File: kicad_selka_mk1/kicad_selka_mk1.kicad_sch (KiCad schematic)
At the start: 76 parts, among them J1 Conn_01x06_Pin, J2 Conn_01x02_Pin, U1 ATtiny861A-S

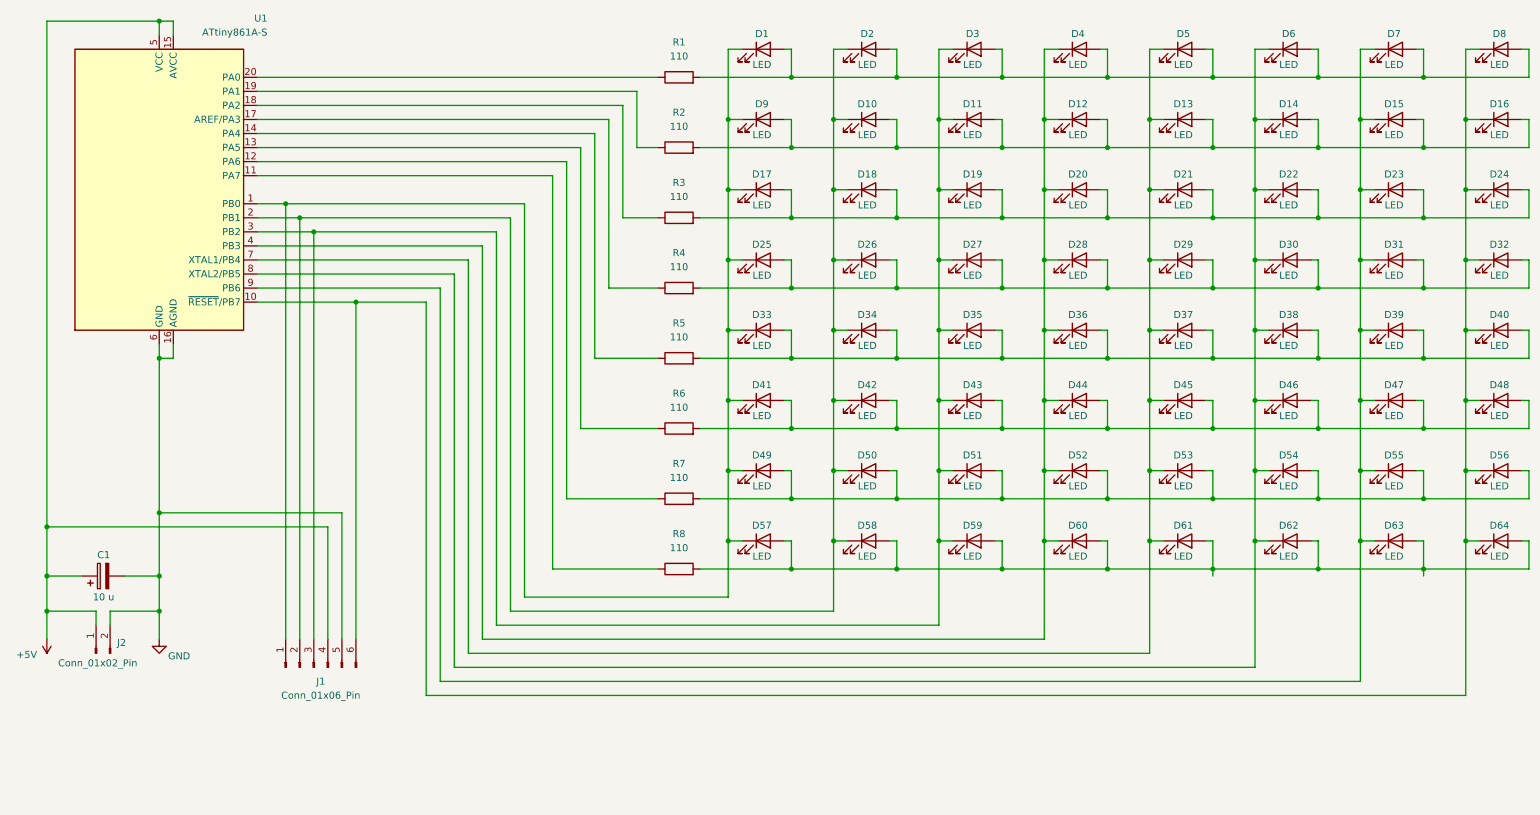
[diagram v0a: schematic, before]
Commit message: Selkäsalaman skemaan lisätty jumperit
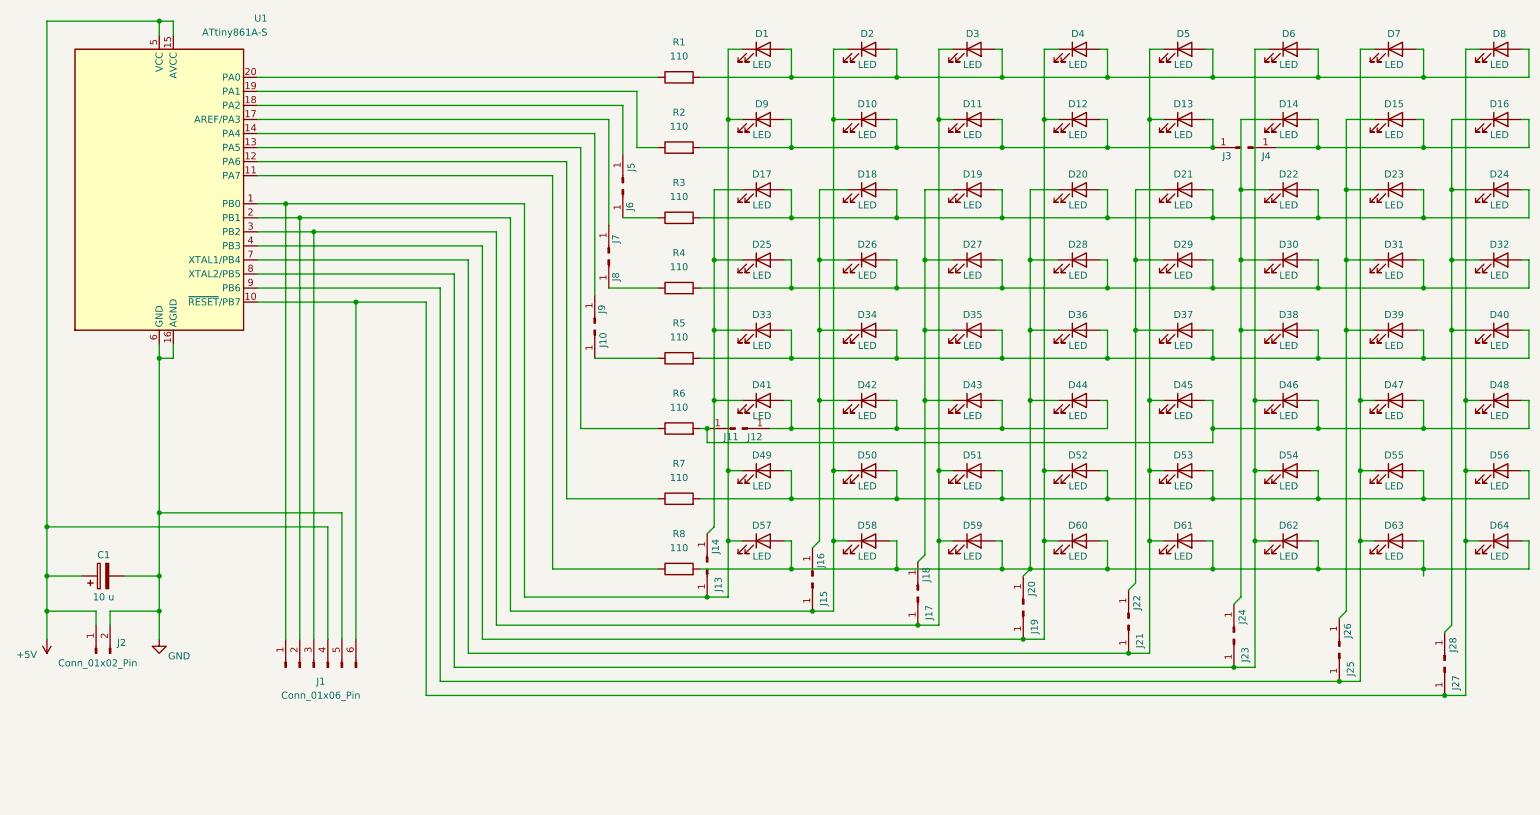
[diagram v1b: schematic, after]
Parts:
- added J10, J11, J12, J13, J14, J15, J16, J17, J18, J19, J20, J21, J22, J23, J24, J25, J26, J27, J28, J3, J4, J5, J6, J7, J8, J9: Conn_01x01_Pin, Connector_PinSocket_2.54mm:PinSocket_1x01_P2.54mm_Vertical, symbol Connector:Conn_01x01_Pin
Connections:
- net at D13.1 (K), D45.1 (K), D5.1 (K)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: now also J21.1 (Pin_1); no longer D21.1 (K), D29.1 (K), D37.1 (K)
- net at D11.1 (K), D3.1 (K), D51.1 (K)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: now also J17.1 (Pin_1); no longer D19.1 (K), D27.1 (K), D35.1 (K), D43.1 (K)
- net at D12.1 (K), D4.1 (K), D52.1 (K)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: now also J19.1 (Pin_1); no longer D20.1 (K), D28.1 (K), D36.1 (K), D44.1 (K)
- net at D10.1 (K), D2.1 (K), D50.1 (K)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: now also J15.1 (Pin_1); no longer D18.1 (K), D26.1 (K), D34.1 (K), D42.1 (K)
- net at D57.2 (A), D58.2 (A), D59.2 (A)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: now also D20.1 (K), D28.1 (K), D36.1 (K), D44.1 (K), J20.1 (Pin_1)
- net at D48.1 (K), D56.1 (K), D64.1 (K)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: now also J27.1 (Pin_1); no longer D16.1 (K), D24.1 (K), D32.1 (K), D40.1 (K)
- net at D47.1 (K), D55.1 (K), D63.1 (K)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: now also J25.1 (Pin_1); no longer D15.1 (K), D23.1 (K), D31.1 (K), D39.1 (K)
- net at D46.1 (K), D54.1 (K), D6.1 (K)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: now also J23.1 (Pin_1); no longer D14.1 (K), D22.1 (K), D30.1 (K), D38.1 (K)
- net at R4.1: now also J8.1 (Pin_1); no longer U1.17 (AREF/PA3)
- net at D45.2 (A), D46.2 (A), D47.2 (A)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: now also J11.1 (Pin_1); no longer D41.2 (A), D42.2 (A), D43.2 (A), D44.2 (A)
- net at D10.2 (A), D11.2 (A), D12.2 (A)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: now also J3.1 (Pin_1); no longer D14.2 (A), D15.2 (A), D16.2 (A)
- net at D1.1 (K), D49.1 (K), D57.1 (K)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: now also J13.1 (Pin_1); no longer D17.1 (K), D25.1 (K), D33.1 (K), D41.1 (K)
- net at R3.1: now also J6.1 (Pin_1); no longer U1.18 (PA2)
- net at R5.1: now also J10.1 (Pin_1); no longer U1.14 (PA4)
- new net: D21.1 (K), D29.1 (K), D37.1 (K), J22.1 (Pin_1)
- new net: D19.1 (K), D27.1 (K), D35.1 (K), D43.1 (K), J18.1 (Pin_1)
- new net: D18.1 (K), D26.1 (K), D34.1 (K), D42.1 (K), J16.1 (Pin_1)
- new net: D16.1 (K), D24.1 (K), D32.1 (K), D40.1 (K), J28.1 (Pin_1)
- new net: D14.1 (K), D22.1 (K), D30.1 (K), D38.1 (K), J24.1 (Pin_1)
- new net: D41.2 (A), D42.2 (A), D43.2 (A), D44.2 (A), J12.1 (Pin_1)
- new net: D17.1 (K), D25.1 (K), D33.1 (K), D41.1 (K), J14.1 (Pin_1)
- new net: D14.2 (A), D15.2 (A), D16.2 (A), J4.1 (Pin_1)
- new net: D15.1 (K), D23.1 (K), D31.1 (K), D39.1 (K), J26.1 (Pin_1)
- new net: J9.1 (Pin_1), U1.14 (PA4)
- new net: J5.1 (Pin_1), U1.18 (PA2)
- new net: J7.1 (Pin_1), U1.17 (AREF/PA3)

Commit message: Selkäsalama 95% done
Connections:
- net at D57.2 (A), D58.2 (A), D59.2 (A)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: no longer D20.1 (K), D28.1 (K), D36.1 (K), D44.1 (K), J20.1 (Pin_1)
- new net: D20.1 (K), D28.1 (K), D36.1 (K), D44.1 (K), J20.1 (Pin_1)
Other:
- note added: "CYAANI ALUE = Alempi Levy"
- moved on the sheet: J10, J11, J12, J13, J14, J15, J16, J17, J18, J19, J20, J21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

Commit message: Selkäsalama redo
1 ledi meni väärälle puolelle -> 31 & 33 lediä :C

Samahan se oli tehdä koko leiska uudelleen parammilla array
ledipaikoilla...
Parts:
- added R9: 110, Resistor_SMD:R_1206_3216Metric_Pad1.30x1.75mm_HandSolder, symbol Device:R
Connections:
- net +5V: now also R9.1
- net GND: now also R9.2
- net at D21.1 (K), D29.1 (K), D37.1 (K)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: now also D45.1 (K)
- net at D13.1 (K), D5.1 (K), D53.1 (K)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: no longer D45.1 (K)
- net at D41.2 (A), D42.2 (A), D43.2 (A)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: now also D45.2 (A)
- net at D46.2 (A), D47.2 (A), D48.2 (A)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: no longer D45.2 (A)
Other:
- title: Salama-64 -> Selkäsalama-64
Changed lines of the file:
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@@
 	(paper "User" 330.2 203.2)
 	(title_block
-		(title "Salama-64")
+		(title "Selkäsalama-64")
 		(date "2026-02-12")
 		(company "ELEKTRONIIKKAKERHO")
@@
 	)
 	(junction
+		(at 226.06 92.71)
+		(diameter 0)
+		(color 0 255 255 1)
+	)
+	(junction
 		(at 290.83 97.79)
 		(diameter 0)
@@
 	)
 	(junction
+		(at 54.61 115.57)
+		(diameter 0)
+		(color 0 0 0 0)
+	)
+	(junction
 		(at 193.04 138.43)
 		(diameter 0)
@@
 	)
 	(junction
-		(at 233.68 97.79)
-		(diameter 0)
-		(color 0 0 0 0)
-	)
-	(junction
 		(at 154.94 85.09)
 		(diameter 0)
@@
 	)
 	(junction
+		(at 34.29 115.57)
+		(diameter 0)
+		(color 0 0 0 0)
+	)
+	(junction
 		(at 212.09 97.79)
 		(diameter 0)
@@
 	)
 	(junction
-		(at 245.11 102.87)
-		(diameter 0)
-		(color 0 0 0 0)
-	)
-	(junction
 		(at 154.94 72.39)
 		(diameter 0)
@@
 	)
 	(junction
+		(at 231.14 97.79)
+		(diameter 0)
+		(color 0 255 255 1)
+	)
+	(junction
 		(at 252.73 97.79)
 		(diameter 0)
@@
 	(wire
 		(pts
-			(xy 233.68 97.79) (xy 236.22 97.79)
-		)
-		(stroke
-			(width 0)
-			(type default)
-		)
-	)
-	(wire
-		(pts
 			(xy 283.21 102.87) (xy 302.26 102.87)
 		)
@@
 	(wire
 		(pts
-			(xy 233.68 46.99) (xy 233.68 97.79)
-		)
-		(stroke
-			(width 0)
-			(type default)
-		)
-	)
-	(wire
-		(pts
 			(xy 264.16 115.57) (xy 283.21 115.57)
 		)
@@
 			(width 0)
 			(type default)
+			(color 0 255 255 1)
 		)
 	)
@@
 	(wire
 		(pts
+			(xy 231.14 97.79) (xy 236.22 97.79)
+		)
+		(stroke
+			(width 0)
+			(type default)
+			(color 0 255 255 1)
+		)
+	)
+	(wire
+		(pts
 			(xy 135.89 52.07) (xy 139.7 52.07)
 		)
@@
 	(wire
 		(pts
+			(xy 245.11 92.71) (xy 245.11 97.79)
+		)
+		(stroke
+			(width 0)
+			(type default)
+			(color 0 255 255 1)
+		)
+	)
+	(wire
+		(pts
 			(xy 168.91 90.17) (xy 187.96 90.17)
 		)
@@
 	(wire
 		(pts
+			(xy 34.29 115.57) (xy 40.64 115.57)
+		)
+		(stroke
+			(width 0)
+			(type default)
+		)
+	)
+	(wire
+		(pts
 			(xy 72.39 77.47) (xy 100.33 77.47)
 		)
@@
 	(wire
 		(pts
+			(xy 54.61 90.17) (xy 54.61 115.57)
+		)
+		(stroke
+			(width 0)
+			(type default)
+		)
+	)
+	(wire
+		(pts
 			(xy 72.39 49.53) (xy 128.27 49.53)
 		)
@@
 	(wire
 		(pts
+			(xy 34.29 29.21) (xy 34.29 115.57)
+		)
+		(stroke
+			(width 0)
+			(type default)
+		)
+	)
+	(wire
+		(pts
 			(xy 130.81 77.47) (xy 139.7 77.47)
 		)
@@
 	(wire
 		(pts
-			(xy 149.86 102.87) (xy 245.11 102.87)
+			(xy 149.86 102.87) (xy 264.16 102.87)
 		)
 		(stroke
@@
 	(wire
 		(pts
+			(xy 48.26 115.57) (xy 54.61 115.57)
+		)
+		(stroke
+			(width 0)
+			(type default)
+		)
+	)
+	(wire
+		(pts
 			(xy 226.06 64.77) (xy 245.11 64.77)
 		)
@@
 	(wire
 		(pts
+			(xy 226.06 92.71) (xy 245.11 92.71)
+		)
+		(stroke
+			(width 0)
+			(type default)
+			(color 0 255 255 1)
+		)
+	)
+	(wire
+		(pts
 			(xy 283.21 123.19) (xy 283.21 128.27)
 		)
@@
 	(wire
 		(pts
-			(xy 231.14 85.09) (xy 231.14 132.08)
+			(xy 231.14 85.09) (xy 231.14 97.79)
 		)
 		(stroke
@@
 	(wire
 		(pts
-			(xy 34.29 120.65) (xy 34.29 29.21)
+			(xy 34.29 120.65) (xy 34.29 115.57)
 		)
 		(stroke
@@
 	(wire
 		(pts
-			(xy 233.68 97.79) (xy 233.68 110.49)
+			(xy 233.68 46.99) (xy 233.68 110.49)
 		)
 		(stroke
@@
 	(wire
 		(pts
-			(xy 54.61 118.11) (xy 54.61 90.17)
+			(xy 54.61 118.11) (xy 54.61 115.57)
 		)
 		(stroke
@@
 	(wire
 		(pts
+			(xy 231.14 97.79) (xy 231.14 132.08)
+		)
+		(stroke
+			(width 0)
+			(type default)
+			(color 0 255 255 1)
+		)
+	)
+	(wire
+		(pts
 			(xy 123.19 115.57) (xy 139.7 115.57)
 		)
@@
 	(wire
 		(pts
-			(xy 245.11 97.79) (xy 245.11 102.87)
-		)
-		(stroke
-			(width 0)
-			(type default)
-		)
-	)
-	(wire
-		(pts
 			(xy 102.87 146.05) (xy 250.19 146.05)
 		)
@@
 	(wire
 		(pts
-			(xy 245.11 102.87) (xy 264.16 102.87)
-		)
-		(stroke
-			(width 0)
-			(type default)
-		)
-	)
-	(wire
-		(pts
 			(xy 207.01 46.99) (xy 207.01 52.07)
 		)
@@
 			(pts
 				(xy 304.8 41.91) (xy 248.92 41.91) (xy 248.92 43.18) (xy 248.92 54.61) (xy 152.4 54.61) (xy 152.4 59.69)
-				(xy 152.4 105.41) (xy 228.6 105.41) (xy 228.6 93.98) (xy 228.6 92.71) (xy 304.8 92.71)
+				(xy 152.4 105.41) (xy 247.65 105.41) (xy 247.65 93.98) (xy 247.65 92.71) (xy 304.8 92.71)
 			)
 			(stroke
@@
 					(unit 1)
 				)
+			)
+		)
+	)
+	(symbol
+		(lib_id "Device:R")
+		(at 44.45 115.57 90)
+		(unit 1)
+		(exclude_from_sim no)
+		(in_bom yes)
+		(on_board yes)
+		(dnp no)
+		(fields_autoplaced yes)
+		(property "Reference" "R9"
+			(at 44.45 109.22 90)
+			(effects
+				(font
+					(size 1.27 1.27)
+				)
+			)
+		)
+		(property "Value" "110"
+			(at 44.45 111.76 90)
+			(effects
+				(font
+					(size 1.27 1.27)
+				)
+			)
+		)
+		(property "Footprint" "Resistor_SMD:R_1206_3216Metric_Pad1.30x1.75mm_HandSolder"
+			(at 44.45 117.348 90)
+			(effects
+				(font
+					(size 1.27 1.27)
+				)
+				(hide yes)
+			)
+		)
+		(property "Datasheet" "~"
+			(at 44.45 115.57 0)
+			(effects
+				(font
+					(size 1.27 1.27)
+				)
+				(hide yes)
+			)
+		)
+		(property "Description" "Resistor"
+			(at 44.45 115.57 0)
+			(effects
+				(font
+					(size 1.27 1.27)
+				)
+				(hide yes)
+			)
+		)
+		(pin "1"
+		)
+		(pin "2"
+		)
+		(instances
+			(project "kicad_selka_mk1"
+				(path "/19c3cedf-93d3-4c6c-b33c-34cff50e8bf3"
+					(reference "R9")
+					(unit 1)
+				)

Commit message: selkäsalama mk1 done
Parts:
- removed J1: Conn_01x06_Pin, Connector_PinHeader_2.00mm:PinHeader_1x06_P2.00mm_Vertical_SMD_Pin1Left, symbol Connector:Conn_01x06_Pin
- added J28, J29, J30, J31: Conn_01x01_Pin, TestPoint:TestPoint_Pad_1.0x1.0mm, symbol Connector:Conn_01x01_Pin
- J4: renamed from J6; footprint Connector_PinSocket_2.54mm:PinSocket_1x01_P2.54mm_Vertical -> Connector_Pin:Pin_D0.7mm_L6.5mm_W1.8mm_FlatFork
- renumbered J3 to J1, J12 to J10, J13 to J11, J14 to J12, J15 to J13, J16 to J14, J17 to J15, J18 to J16, J19 to J17, J20 to J18, J21 to J19, J4 to J2, J22 to J20, J23 to J21, J24 to J22, J25 to J23, J26 to J24, J27 to J25, J28 to J26, J2 to J27, J5 to J3, J7 to J5, J8 to J6, J9 to J7, J10 to J8, J11 to J9
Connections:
- net at D10.1 (K), D2.1 (K), D50.1 (K)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: now also J29.1 (Pin_1)
- net at D11.1 (K), D3.1 (K), D51.1 (K)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: now also J30.1 (Pin_1)
- net at D1.1 (K), D49.1 (K), D57.1 (K)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: now also J28.1 (Pin_1)
- net at D48.1 (K), D56.1 (K), D64.1 (K)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: now also J31.1 (Pin_1)

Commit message: selkäsalama mk1 rev 2
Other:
- moved on the sheet: C1, J27, R9
